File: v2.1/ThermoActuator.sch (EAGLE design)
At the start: 82 parts, among them IC1 PCF8574T, IC2 ULN2003AD, IC3 REG1117, Q1 200mA/50V, Q2 200mA/50V, U1 CD74HCT4051_D_16

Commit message: ThermoShield v2.1
a new version with WiFi support and cloud capabilities
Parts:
- removed 1, 2, 3, 4, 5, 6, 7, 8: (no value), led:LEDCHIP-LED0805
- removed C2, C3, C4, C5, C6, C7: 5uF, SparkFun-Capacitors:CAP_POL1206
- removed D1: 1N4001, diode:DIODE-D-10
- removed JP11, JP12, JP13, JP14, JP2, JP23, JP24, JP3, JP4: M025MM, SparkFun-Connectors:M025MM
- removed R10, R11, R12: 1K, rcl:R-EU_R1206
- removed R14, R15, R16, R17, R18, R19, R20, R21: 3K3, rcl:R-EU_R0805
- removed R27: 10K, resistor:R-EU_R0805
- added G1: CH291-1220LF, battery:CH291-1220LF
- added IC4: DS1307, dallas-1:DS1307
- added Q3: MOSFET-NCHANNEL_DUAL, lio:MOSFET-NCHANNEL_DUAL
- added U2: AD5165BUJZ100-R2, AD5165_DigitalPot:AD5165BUJZ100-R2
- added U3: LTC4365CTS8TRMPBF, LTC_By_element14_Batch_1:LTC4365CTS8TRMPBF
- added X10, X11, X2, X3, X4, X5, X6, X7, X8, X9: (no value), con-phoenix-500:MSTBV2
- added Y1: (no value), SparkFun-FreqCtrl:CRYSTAL3.2X1.5MM
- C1: value 5uF -> 100nF; device SparkFun-Capacitors:CAP_POL1206 -> rcl:C-EUC0805
- JP1: value M025MM -> (none); device SparkFun-Connectors:M025MM -> pinhead:PINHD-1X3
- R1: value 1K -> 100K; device rcl:R-EU_R1206 -> rcl:R-EU_R0805
- R2: value 1K -> 1.82M; device rcl:R-EU_R1206 -> rcl:R-EU_R0805
- R3, R4: value 1K -> 150K; device rcl:R-EU_R1206 -> rcl:R-EU_R0805
- renumbered R8 to R8*, R9 to R9*
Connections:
- removed net D51: JP26.2
- removed net D52: JP27.16
- removed net N$16: 4.A, R17.1
- removed net N$17: 5.A, R18.1
- removed net N$18: 6.A, R19.1
- removed net N$19: 7.A, R20.1
- removed net N$23: JP14.2, R13.1
- removed net N$32: 8.A, R21.1
- new net D51(MOSI): JP26.2, U2.SDI
- new net D52(SCLK): JP27.16, U2.CLK
- net AO0: no longer 1.C
- net AO1: no longer 2.C
- net AO2: no longer 3.C
- net AO3: no longer 4.C
- net AO4: no longer 5.C
- net AO5: no longer 6.C
- net AO6: no longer 7.C
- net AO7: no longer 8.C
- net AS0: now also X4-1.SK; no longer C1.+, R1.2
- net AS1: now also X5-1.SK; no longer C2.+, R2.2
- net AS2: now also X6-1.SK; no longer C3.+, R3.2
- net AS3: now also X7-1.SK; no longer C4.+, R4.2
- net AS4: now also X8-1.SK; no longer C5.+, R10.2
- net AS5: now also X9-1.SK; no longer C6.+, R11.2
- net AS6: now also X10-1.SK; no longer C7.+, R12.2
- net AS7: now also X11-1.SK; no longer C8.+, R13.2
- net D11: now also U2.CS
- net GND: now also C1.2, G1.-, JP1.3, R4.1, U2.GND, U3.GND, X10-2.SK, X11-2.SK, X3-1.SK, X3-2.SK, X4-2.SK, X5-2.SK, X6-2.SK, X7-2.SK, X8-2.SK, X9-2.SK; no longer C1.-, C2.-, C3.-, C4.-, C5.-, C6.-, C7.-, JP1.1, JP11.1, JP12.1, JP13.1, JP14.1, JP2.1, JP24.1, JP24.2, JP3.1, JP4.1
- net N$1: now also U3.~SHDN; no longer JP1.2
- net N$11: now also IC4.GND; no longer JP3.2, R3.1
- net N$12: now also R2.1, R3.2, U3.UV; no longer JP4.2, R4.1
- net N$13: now also R3.1, R4.2, U3.OV; no longer 1.A, R14.1
- net N$14: now also Q3A.G, Q3B.G, U3.GATE; no longer 2.A, R15.1
- net N$15: now also Q3A.S, Q3B.S; no longer 3.A, R16.1
- net N$2: now also R13.2, U1.A, U2.W; no longer JP2.2, R2.1
- net N$20: now also IC4.X1, Y1.2; no longer JP11.2, R10.1
- net N$21: now also IC4.X2, Y1.1; no longer JP12.2, R11.1
- net N$22: now also G1.+, IC4.VBAT; no longer JP13.2, R12.1
- net N$36: now also C8.+, R13.1; no longer R27.1, U1.A
- net N$42: now also Q3A.D1, R1.2, R2.2, U3.VIN; no longer D1.A
- net RX1: now also JP1.2
- net SCL: now also IC4.SCL
- net SDA: now also IC4.SDA
- net TX1: now also JP1.1
- net VDD: now also C1.1, IC4.VCC, Q3B.D1, U2.A, U2.VDD, U3.VOUT, X2-1.SK, X2-2.SK; no longer D1.C, JP23.1, JP23.2, R14.2, R15.2, R16.2, R17.2, R18.2, R19.2, R20.2, R21.2, R27.2
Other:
- note added: "* R8 and R9 are populated on the master board only"
- note added: "256-step Digital pot Voltage Divider"
- note added: "All the pins on JP10 (except serial 0) and JP27 (except SPI) are reserved for the LCD touch screen D8,D9,D10 - MUX control D11 - SS for digital pot"
- note added: "Debug serial connector Serial1"
- note added: "Low-Pass Filter"
- note added: "RTC circuit"
- note added: "The dual N-MOSFET used for this design is SI4946BEY. Continuous drain current about 5A"
- note added: "Two extra contacts for VDD and GND primarily to connect the relay board"
- note removed: "* R18 and R19 are populated on the master board only"
- note removed: "All the pins on JP4 and JP17 headers are reserved for the LCD touch screen"
- note removed: "LED1"
- note removed: "LED8"
- note removed: "Relay control LEDs"
- note removed: "Voltage Divider 1% precision or better"
- moved on the sheet: C14, C8, J1, JP8, JP9, R1, R13, R2, R3, R4, U1

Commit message: routing complete, LEDs are back
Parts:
- removed JP1: (no value), pinhead:PINHD-1X3
- added 1, 2, 3, 4, 5, 6, 7, 8: (no value), led:LEDCHIP-LED0805
- added JP2: (no value), pinhead:PINHD-1X2
- added R10, R11, R12, R14, R15, R16, R8, R9: 3K3, rcl:R-EU_R0805
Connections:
- new net N$23: 2.A, R9.1
- new net N$32: 3.A, R10.1
- new net N$46: 4.A, R11.1
- new net N$47: 5.A, R12.1
- new net N$48: 6.A, R14.1
- new net N$49: 7.A, R15.1
- new net N$50: 8.A, R16.1
- net AO0: now also 1.C
- net AO1: now also 2.C
- net AO2: now also 3.C
- net AO3: now also 4.C
- net AO4: now also 5.C
- net AO5: now also 6.C
- net AO6: now also 7.C
- net AO7: now also 8.C
- net GND: now also IC4.GND; no longer JP1.3
- net N$11: now also 1.A, R8.1; no longer IC4.GND
- net RX1: now also JP2.2; no longer JP1.2
- net TX1: now also JP2.1; no longer JP1.1
- net VDD: now also R10.2, R11.2, R12.2, R14.2, R15.2, R16.2, R8.2, R9.2
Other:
- note added: "Debug serial connector Serial1. Use the X3-x connector for GND if the header is covered by an LCD shield"
- note added: "Output signal LEDs. The LEDs and the current limitting resistors are only mounted if the standard blue terminals are used. For the 90 degree terminals, leave unpopulated"
- note added: "RTC circuit, as well as the battery are mounted on master board only"
- note removed: "Debug serial connector Serial1"
- moved on the sheet: G1, IC4, J1, Q3A, Q3B, R1, R2, R3, R4, U3, Y1

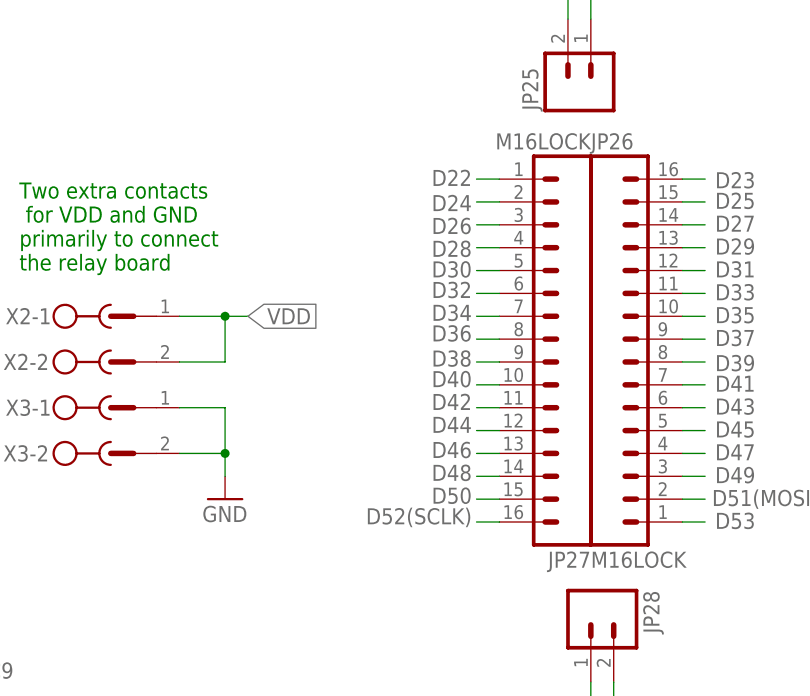
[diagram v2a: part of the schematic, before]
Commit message: Digital Pot AD5165
apart from the simple support for the digital POT, it was
discovered that the double row header 38-pin was not correctly
pin-mapped on the shield. This caused the SPI CLK would be
connected to D22, instead of D52. Now, this is corrected, but...
too late:)
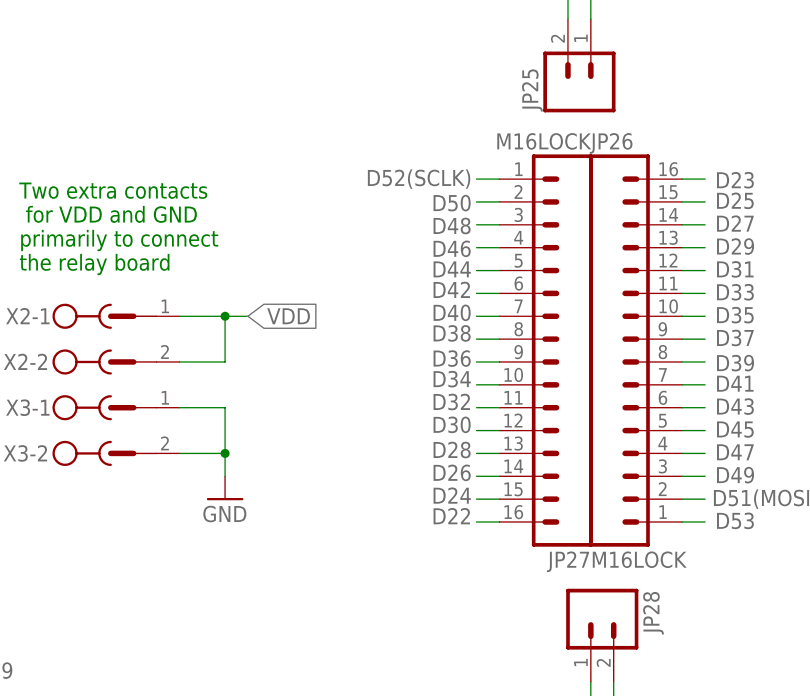
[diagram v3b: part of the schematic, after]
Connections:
- net D22: now also JP27.16; no longer JP27.1
- net D24: now also JP27.15; no longer JP27.2
- net D26: now also JP27.14; no longer JP27.3
- net D28: now also JP27.13; no longer JP27.4
- net D30: now also JP27.12; no longer JP27.5
- net D32: now also JP27.11; no longer JP27.6
- net D34: now also JP27.10; no longer JP27.7
- net D36: now also JP27.9; no longer JP27.8
- net D38: now also JP27.8; no longer JP27.9
- net D40: now also JP27.7; no longer JP27.10
- net D42: now also JP27.6; no longer JP27.11
- net D44: now also JP27.5; no longer JP27.12
- net D46: now also JP27.4; no longer JP27.13
- net D48: now also JP27.3; no longer JP27.14
- net D50: now also JP27.2; no longer JP27.15
- net D52(SCLK): now also JP27.1; no longer JP27.16
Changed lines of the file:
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@@
 <?xml version="1.0" encoding="utf-8"?>
 <!DOCTYPE eagle SYSTEM "eagle.dtd">
-<eagle version="7.4.0">
+<eagle version="7.1.0">
 <drawing>
 <settings>
@@
 <net name="D22" class="0">
 <segment>
+<wire x1="165.1" y1="76.2" x2="167.64" y2="76.2" width="0.1524" layer="91"/>
+<label x="164.592" y="77.724" size="1.778" layer="95" rot="R180"/>
+<pinref part="JP27" gate="G$1" pin="16"/>
+</segment>
+</net>
+<net name="D38" class="0">
+<segment>
+<wire x1="165.1" y1="96.52" x2="167.64" y2="96.52" width="0.1524" layer="91"/>
+<label x="164.592" y="98.044" size="1.778" layer="95" rot="R180"/>
+<pinref part="JP27" gate="G$1" pin="8"/>
+</segment>
+</net>
+<net name="D40" class="0">
+<segment>
+<wire x1="165.1" y1="99.06" x2="167.64" y2="99.06" width="0.1524" layer="91"/>
+<label x="164.592" y="100.33" size="1.778" layer="95" rot="R180"/>
+<pinref part="JP27" gate="G$1" pin="7"/>
+</segment>
+</net>
+<net name="D42" class="0">
+<segment>
+<wire x1="165.1" y1="101.6" x2="167.64" y2="101.6" width="0.1524" layer="91"/>
+<label x="164.592" y="102.87" size="1.778" layer="95" rot="R180"/>
+<pinref part="JP27" gate="G$1" pin="6"/>
+</segment>
+</net>
+<net name="D44" class="0">
+<segment>
+<wire x1="165.1" y1="104.14" x2="167.64" y2="104.14" width="0.1524" layer="91"/>
+<label x="164.592" y="105.156" size="1.778" layer="95" rot="R180"/>
+<pinref part="JP27" gate="G$1" pin="5"/>
+</segment>
+</net>
+<net name="D46" class="0">
+<segment>
+<wire x1="165.1" y1="106.68" x2="167.64" y2="106.68" width="0.1524" layer="91"/>
+<label x="164.592" y="107.442" size="1.778" layer="95" rot="R180"/>
+<pinref part="JP27" gate="G$1" pin="4"/>
+</segment>
+</net>
+<net name="D48" class="0">
+<segment>
+<wire x1="165.1" y1="109.22" x2="167.64" y2="109.22" width="0.1524" layer="91"/>
+<label x="164.592" y="109.982" size="1.778" layer="95" rot="R180"/>
+<pinref part="JP27" gate="G$1" pin="3"/>
+</segment>
+</net>
+<net name="D50" class="0">
+<segment>
+<wire x1="165.1" y1="111.76" x2="167.64" y2="111.76" width="0.1524" layer="91"/>
+<label x="164.592" y="112.522" size="1.778" layer="95" rot="R180"/>
+<pinref part="JP27" gate="G$1" pin="2"/>
+</segment>
+</net>
+<net name="D52(SCLK)" class="0">
+<segment>
+<pinref part="U2" gate="A" pin="CLK"/>
+<wire x1="40.64" y1="-119.38" x2="38.1" y2="-119.38" width="0.1524" layer="91"/>
+<label x="38.1" y="-119.38" size="1.778" layer="95" rot="R180"/>
+</segment>
+<segment>
 <wire x1="165.1" y1="114.3" x2="167.64" y2="114.3" width="0.1524" layer="91"/>
 <label x="164.592" y="115.316" size="1.778" layer="95" rot="R180"/>
 <pinref part="JP27" gate="G$1" pin="1"/>
-</segment>
-</net>
-<net name="D24" class="0">
-<segment>
-<wire x1="165.1" y1="111.76" x2="167.64" y2="111.76" width="0.1524" layer="91"/>
-<label x="164.592" y="112.522" size="1.778" layer="95" rot="R180"/>
-<pinref part="JP27" gate="G$1" pin="2"/>
-</segment>
-</net>
-<net name="D26" class="0">
-<segment>
-<wire x1="165.1" y1="109.22" x2="167.64" y2="109.22" width="0.1524" layer="91"/>
-<label x="164.592" y="109.982" size="1.778" layer="95" rot="R180"/>
-<pinref part="JP27" gate="G$1" pin="3"/>
-</segment>
-</net>
-<net name="D28" class="0">
-<segment>
-<wire x1="165.1" y1="106.68" x2="167.64" y2="106.68" width="0.1524" layer="91"/>
-<label x="164.592" y="107.442" size="1.778" layer="95" rot="R180"/>
-<pinref part="JP27" gate="G$1" pin="4"/>
-</segment>
-</net>
-<net name="D30" class="0">
-<segment>
-<wire x1="165.1" y1="104.14" x2="167.64" y2="104.14" width="0.1524" layer="91"/>
-<label x="164.592" y="105.156" size="1.778" layer="95" rot="R180"/>
-<pinref part="JP27" gate="G$1" pin="5"/>
-</segment>
-</net>
-<net name="D32" class="0">
-<segment>
-<wire x1="165.1" y1="101.6" x2="167.64" y2="101.6" width="0.1524" layer="91"/>
-<label x="164.592" y="102.87" size="1.778" layer="95" rot="R180"/>
-<pinref part="JP27" gate="G$1" pin="6"/>
-</segment>
-</net>
-<net name="D34" class="0">
-<segment>
-<wire x1="165.1" y1="99.06" x2="167.64" y2="99.06" width="0.1524" layer="91"/>
-<label x="164.592" y="100.33" size="1.778" layer="95" rot="R180"/>
-<pinref part="JP27" gate="G$1" pin="7"/>
-</segment>
-</net>
-<net name="D36" class="0">
-<segment>
-<wire x1="165.1" y1="96.52" x2="167.64" y2="96.52" width="0.1524" layer="91"/>
-<label x="164.592" y="98.044" size="1.778" layer="95" rot="R180"/>
-<pinref part="JP27" gate="G$1" pin="8"/>
-</segment>
-</net>
-<net name="D38" class="0">
-<segment>
-<wire x1="165.1" y1="93.98" x2="167.64" y2="93.98" width="0.1524" layer="91"/>
-<label x="164.592" y="95.25" size="1.778" layer="95" rot="R180"/>
-<pinref part="JP27" gate="G$1" pin="9"/>
-</segment>
-</net>
-<net name="D40" class="0">
-<segment>
-<wire x1="165.1" y1="91.44" x2="167.64" y2="91.44" width="0.1524" layer="91"/>
-<label x="164.592" y="92.964" size="1.778" layer="95" rot="R180"/>
-<pinref part="JP27" gate="G$1" pin="10"/>
-</segment>
-</net>
-<net name="D42" class="0">
-<segment>
-<wire x1="165.1" y1="88.9" x2="167.64" y2="88.9" width="0.1524" layer="91"/>
-<label x="164.592" y="90.424" size="1.778" layer="95" rot="R180"/>
-<pinref part="JP27" gate="G$1" pin="11"/>
-</segment>
-</net>
-<net name="D44" class="0">
-<segment>
-<wire x1="165.1" y1="86.36" x2="167.64" y2="86.36" width="0.1524" layer="91"/>
-<label x="164.592" y="87.884" size="1.778" layer="95" rot="R180"/>
-<pinref part="JP27" gate="G$1" pin="12"/>
-</segment>
-</net>
-<net name="D46" class="0">
-<segment>
-<wire x1="165.1" y1="83.82" x2="167.64" y2="83.82" width="0.1524" layer="91"/>
-<label x="164.592" y="85.09" size="1.778" layer="95" rot="R180"/>
-<pinref part="JP27" gate="G$1" pin="13"/>
-</segment>
-</net>
-<net name="D48" class="0">
-<segment>
-<wire x1="165.1" y1="81.28" x2="167.64" y2="81.28" width="0.1524" layer="91"/>
-<label x="164.592" y="82.55" size="1.778" layer="95" rot="R180"/>
-<pinref part="JP27" gate="G$1" pin="14"/>
-</segment>
-</net>
-<net name="D50" class="0">
-<segment>
-<wire x1="165.1" y1="78.74" x2="167.64" y2="78.74" width="0.1524" layer="91"/>
-<label x="164.592" y="80.01" size="1.778" layer="95" rot="R180"/>
-<pinref part="JP27" gate="G$1" pin="15"/>
-</segment>
-</net>
-<net name="D52(SCLK)" class="0">
-<segment>
-<wire x1="165.1" y1="76.2" x2="167.64" y2="76.2" width="0.1524" layer="91"/>
-<label x="164.592" y="77.724" size="1.778" layer="95" rot="R180"/>
-<pinref part="JP27" gate="G$1" pin="16"/>
-</segment>
-<segment>
-<pinref part="U2" gate="A" pin="CLK"/>
-<wire x1="40.64" y1="-119.38" x2="38.1" y2="-119.38" width="0.1524" layer="91"/>
-<label x="38.1" y="-119.38" size="1.778" layer="95" rot="R180"/>
 </segment>
 </net>
@@
 </segment>
 </net>
+<net name="D24" class="0">
+<segment>
+<wire x1="165.1" y1="78.74" x2="167.64" y2="78.74" width="0.1524" layer="91"/>
+<label x="164.592" y="80.01" size="1.778" layer="95" rot="R180"/>
+<pinref part="JP27" gate="G$1" pin="15"/>
+</segment>
+</net>
+<net name="D26" class="0">
+<segment>
+<wire x1="165.1" y1="81.28" x2="167.64" y2="81.28" width="0.1524" layer="91"/>
+<label x="164.592" y="82.55" size="1.778" layer="95" rot="R180"/>
+<pinref part="JP27" gate="G$1" pin="14"/>
+</segment>
+</net>
+<net name="D28" class="0">
+<segment>
+<wire x1="165.1" y1="83.82" x2="167.64" y2="83.82" width="0.1524" layer="91"/>
+<label x="164.592" y="85.09" size="1.778" layer="95" rot="R180"/>
+<pinref part="JP27" gate="G$1" pin="13"/>
+</segment>
+</net>
+<net name="D30" class="0">
+<segment>
+<wire x1="165.1" y1="86.36" x2="167.64" y2="86.36" width="0.1524" layer="91"/>
+<label x="164.592" y="87.884" size="1.778" layer="95" rot="R180"/>
+<pinref part="JP27" gate="G$1" pin="12"/>
+</segment>
+</net>
+<net name="D32" class="0">
+<segment>
+<wire x1="165.1" y1="88.9" x2="167.64" y2="88.9" width="0.1524" layer="91"/>
+<label x="164.592" y="90.424" size="1.778" layer="95" rot="R180"/>
+<pinref part="JP27" gate="G$1" pin="11"/>
+</segment>
+</net>
+<net name="D34" class="0">
+<segment>
+<wire x1="165.1" y1="91.44" x2="167.64" y2="91.44" width="0.1524" layer="91"/>
+<label x="164.592" y="92.964" size="1.778" layer="95" rot="R180"/>
+<pinref part="JP27" gate="G$1" pin="10"/>
+</segment>
+</net>
+<net name="D36" class="0">
+<segment>
+<wire x1="165.1" y1="93.98" x2="167.64" y2="93.98" width="0.1524" layer="91"/>
+<label x="164.592" y="95.25" size="1.778" layer="95" rot="R180"/>
+<pinref part="JP27" gate="G$1" pin="9"/>
+</segment>
+</net>
